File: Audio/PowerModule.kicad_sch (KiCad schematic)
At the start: 15 parts, among them J4 PWR_IN, J5 PWR_OUT

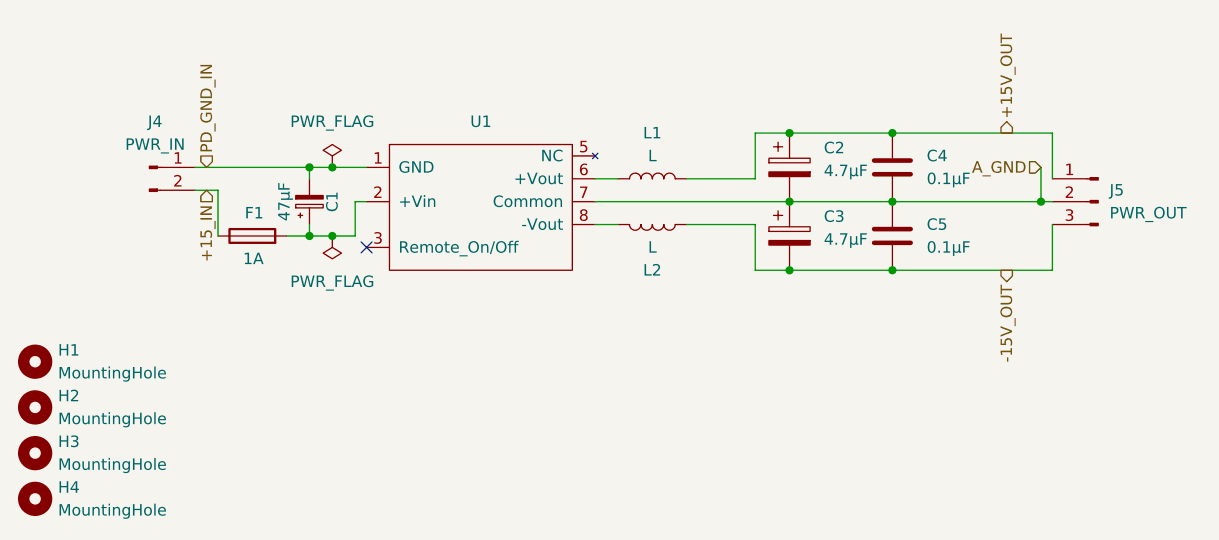
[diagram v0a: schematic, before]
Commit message: Audio: Controll端子・リレー配線とPCB部品配置まで反映。
ControllにAmp向け2P端子10個とリレー周りの回路を更新し、AudioCaseへフットプリントを配置。EQ/Amp/Controllは回路図レイアウトに合わせて部品位置を調整（PowerModuleは配線済みのため未変更）。BP5293-50フットプリント修正と配置用スクリプトを追加。

Co-authored-by: Cursor <cursoragent@cursor.com>
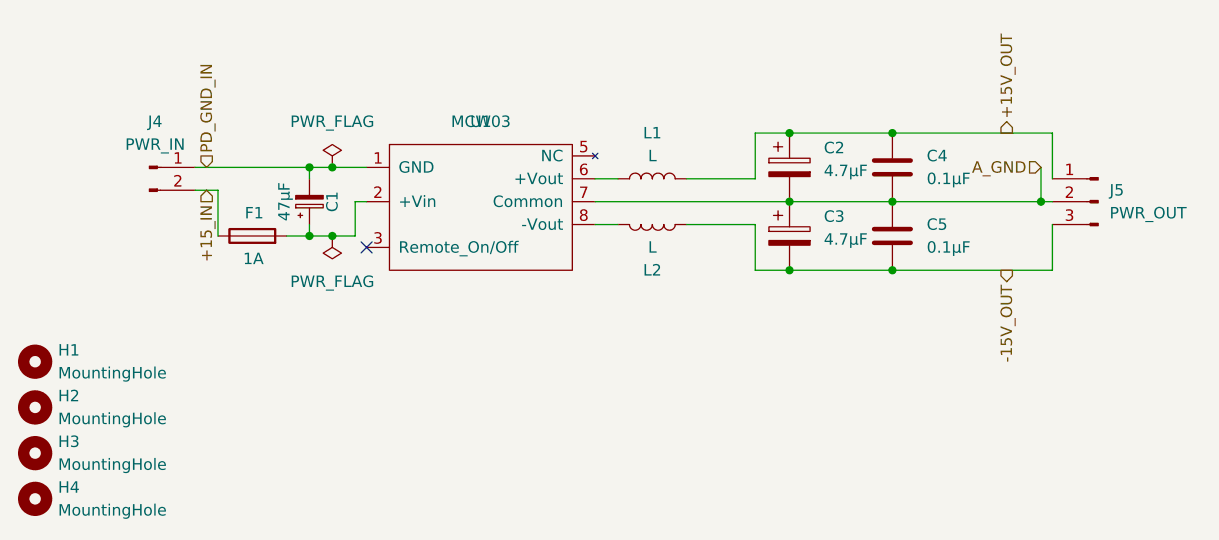
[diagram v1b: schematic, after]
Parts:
- U1: value (none) -> MCW03
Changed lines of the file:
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@@
 			)
 		)
-		(property "Value" ""
+		(property "Value" "MCW03"
 			(at 64.77 31.75 0)
 			(show_name no)
@@
 		(dnp no)
 		(fields_autoplaced yes)
-		(property "Reference" "#FLG08"
+		(property "Reference" "#FLG02"
 			(at 48.26 34.925 0)
 			(hide yes)
@@
 			(project "AudioCase"
 				(path "/760b9589-09e7-434e-9ca2-6e4136e3b7a2/c17b312b-fe0a-430c-8356-b220c9b28aff"
-					(reference "#FLG08")
-					(unit 1)
-				)
+					(reference "#FLG02")
+					(unit 1)
+				)
